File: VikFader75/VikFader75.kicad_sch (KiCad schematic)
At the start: 15 parts, among them J1 vik-module-connector, J2 Conn_01x06_Pin, Q1 DMG2305UX, U1 ADS1115IDGS

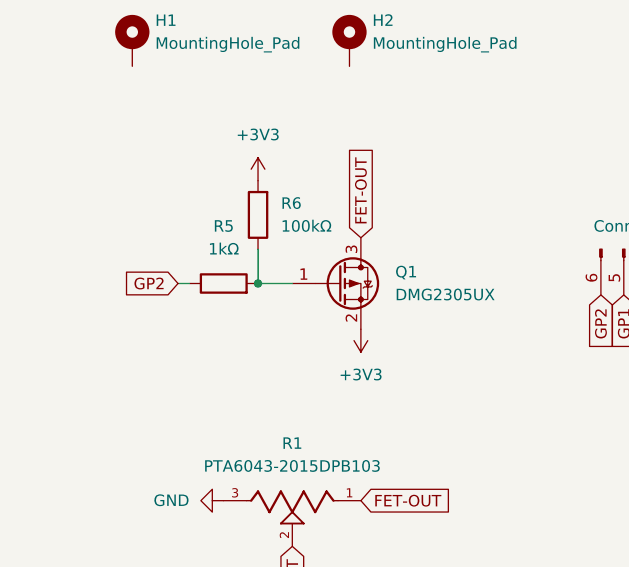
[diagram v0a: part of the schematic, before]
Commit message: All three models refactored to MOSFET setup
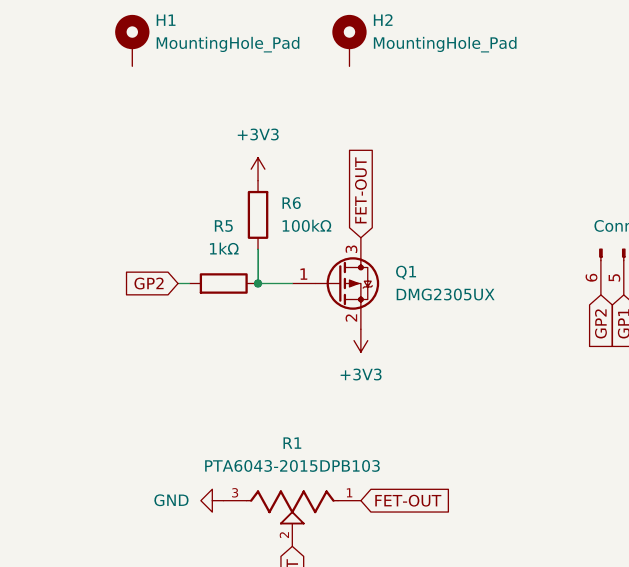
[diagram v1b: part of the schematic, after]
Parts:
- R2, R3, R7: footprint Capacitor_SMD:C_0603_1608Metric -> Resistor_SMD:R_0805_2012Metric
- R4, R5, R6: footprint Capacitor_SMD:C_0603_1608Metric -> Resistor_SMD:R_0603_1608Metric
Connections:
- net GP2: now also R5.2; no longer R5.1
- net at Q1.1 (G), R6.1: now also R5.1; no longer R5.2
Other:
- moved on the sheet: R5
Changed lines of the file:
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@@
 			)
 		)
-		(property "Footprint" "Capacitor_SMD:C_0603_1608Metric"
+		(property "Footprint" "Resistor_SMD:R_0805_2012Metric"
 			(at 92.202 68.58 90)
 			(effects
@@
 			)
 		)
-		(property "Footprint" "Capacitor_SMD:C_0603_1608Metric"
+		(property "Footprint" "Resistor_SMD:R_0603_1608Metric"
 			(at 44.958 82.55 90)
 			(effects
@@
 			)
 		)
-		(property "Footprint" "Capacitor_SMD:C_0603_1608Metric"
+		(property "Footprint" "Resistor_SMD:R_0805_2012Metric"
 			(at 56.642 31.75 90)
 			(effects
@@
 			)
 		)
-		(property "Footprint" "Capacitor_SMD:C_0603_1608Metric"
+		(property "Footprint" "Resistor_SMD:R_0805_2012Metric"
 			(at 89.662 68.58 90)
 			(effects
@@
 	(symbol
 		(lib_id "Device:R")
-		(at 39.37 90.17 90)
-		(unit 1)
-		(exclude_from_sim no)
-		(in_bom yes)
-		(on_board yes)
-		(dnp no)
-		(fields_autoplaced yes)
+		(at 39.37 90.17 270)
+		(mirror x)
+		(unit 1)
+		(exclude_from_sim no)
+		(in_bom yes)
+		(on_board yes)
+		(dnp no)
 		(property "Reference" "R5"
 			(at 39.37 83.82 90)
@@
 			)
 		)
-		(property "Footprint" "Capacitor_SMD:C_0603_1608Metric"
+		(property "Footprint" "Resistor_SMD:R_0603_1608Metric"
 			(at 39.37 91.948 90)
 			(effects
@@
 			)
 		)
-		(property "Footprint" "Capacitor_SMD:C_0603_1608Metric"
+		(property "Footprint" "Resistor_SMD:R_0603_1608Metric"
 			(at 44.45 144.018 90)
 			(effects
